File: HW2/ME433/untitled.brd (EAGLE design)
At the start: 50 x 50 mm, 19 parts, among them SW1 DIP-SLIDE-SWITCH(3P-11.6X4.0X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

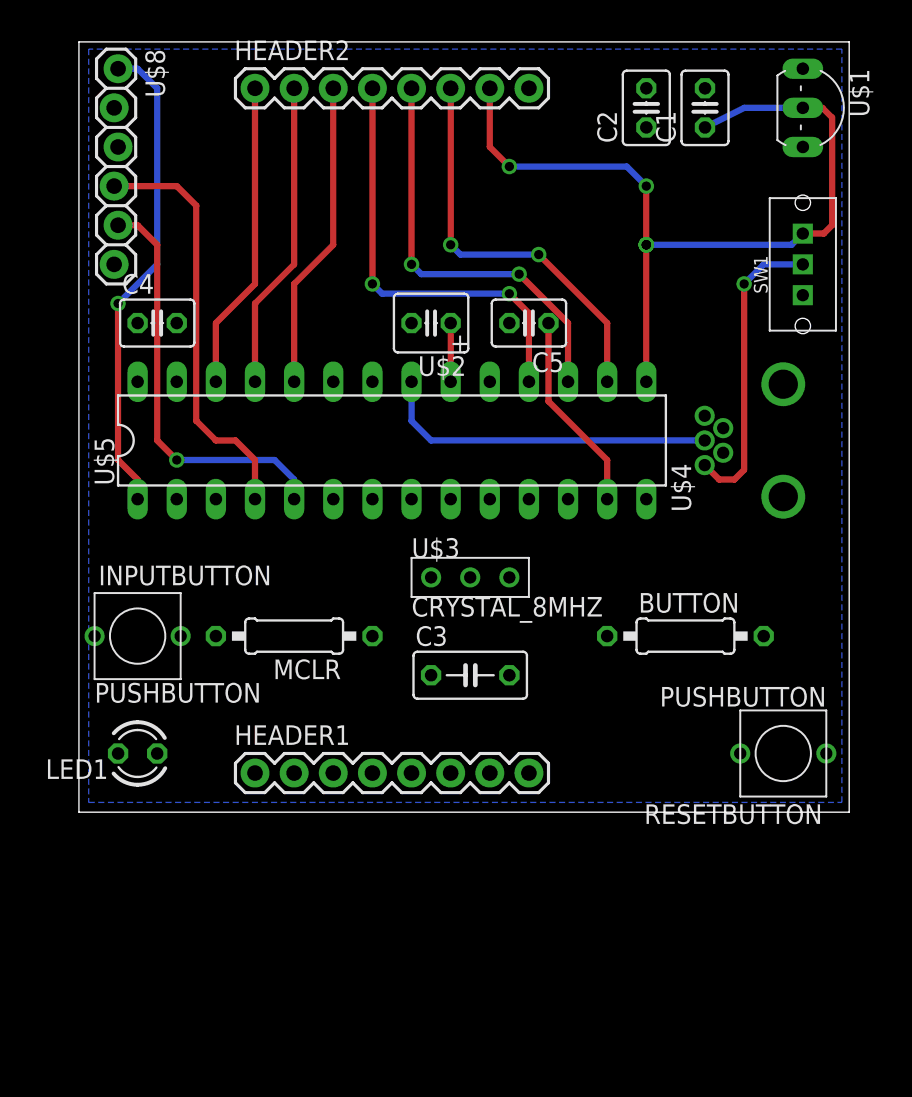
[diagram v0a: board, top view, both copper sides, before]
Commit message: wide traces
wider power traces
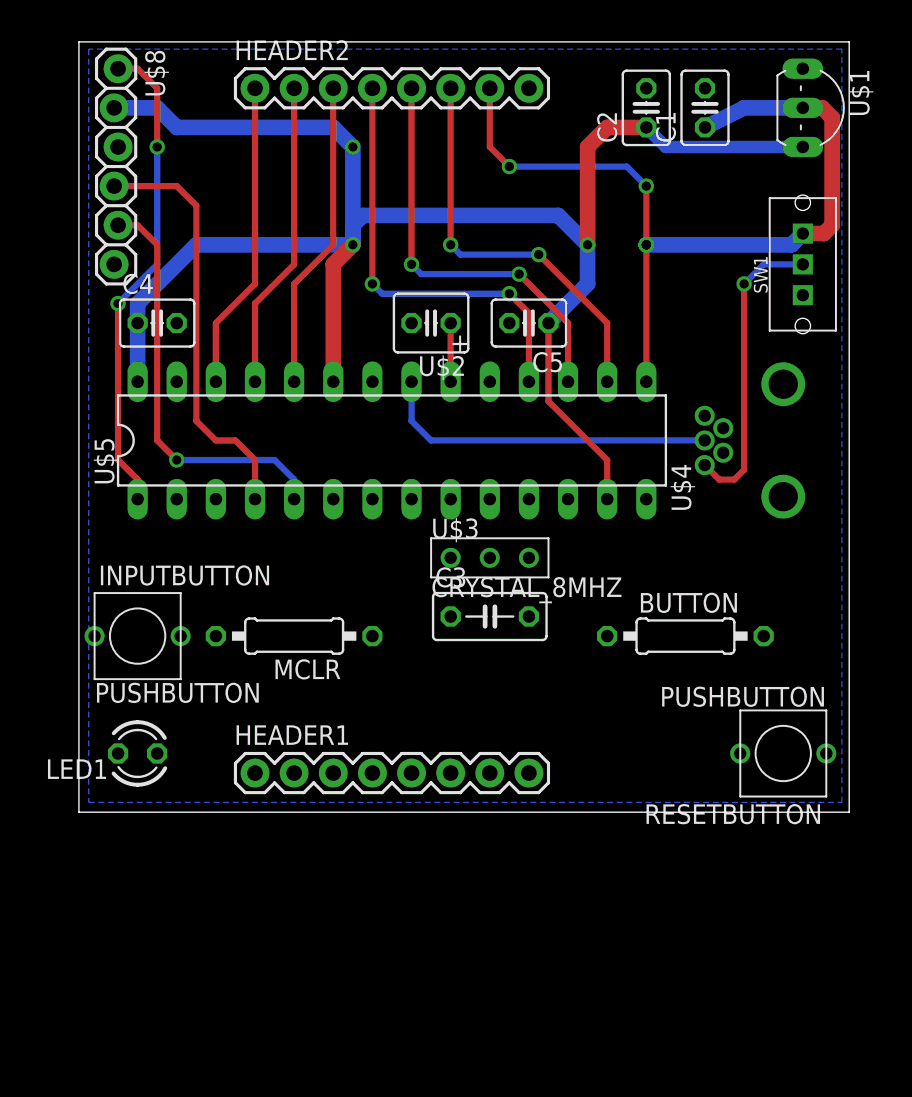
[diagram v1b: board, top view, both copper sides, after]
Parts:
- moved C3 4.02 mm to (26.7, 12.7)
- moved U$3 1.80 mm to (26.7, 16.5)
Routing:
- net +3V3: track 13.0 -> 114.8 mm, vias 0 -> 3
- net MCLR: vias 1 -> 2
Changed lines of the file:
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@@
 <element name="C1" library="components" package="C025-030X050" value="1uf" x="40.64" y="45.72" rot="R90"/>
 <element name="C2" library="components" package="C025-030X050" value="1uf" x="36.83" y="45.72" rot="R90"/>
-<element name="C3" library="components" package="C050-030X075" value=".1uf" x="25.4" y="8.89"/>
+<element name="C3" library="components" package="C050-030X075" value=".1uf" x="26.67" y="12.7"/>
 <element name="C4" library="components" package="C025-030X050" value=".1uf" x="5.08" y="31.75"/>
 <element name="C5" library="components" package="C025-030X050" value=".1uf" x="29.21" y="31.75" rot="R180"/>
@@
 <element name="U$1" library="components" package="TO92-EBC" value="VOLTAGE_REGULATOR_MCP1702" x="48.26" y="45.72" rot="R270"/>
 <element name="U$2" library="components" package="C025-040X050POL" value="CAP_TANT_10UFSHORT" x="22.86" y="31.75" rot="R180"/>
-<element name="U$3" library="components" package="CRYSTAL_8MHZ" value="CRYSTAL_8MHZ" x="25.4" y="15.24"/>
+<element name="U$3" library="components" package="CRYSTAL_8MHZ" value="CRYSTAL_8MHZ" x="26.67" y="16.51"/>
 <element name="U$4" library="components" package="USB-MB-H" value="MICROUSB_BREAKOUTUSBMICROMBH" x="45.72" y="24.13" rot="R180"/>
 <element name="U$5" library="components" package="DIL28-3" value="PIC32MX250F128B" x="20.32" y="24.13"/>
@@
 <wire x1="30.48" y1="26.67" x2="34.29" y2="22.86" width="0.4064" layer="1"/>
 <wire x1="34.29" y1="22.86" x2="34.29" y2="20.32" width="0.4064" layer="1"/>
-<wire x1="36.83" y1="44.45" x2="46.99" y2="43.18" width="0" layer="19" extent="1-1"/>
-<wire x1="30.48" y1="31.75" x2="36.83" y2="44.45" width="0" layer="19" extent="1-1"/>
-<wire x1="34.29" y1="11.43" x2="34.29" y2="20.32" width="0" layer="19" extent="1-1"/>
-<wire x1="22.86" y1="8.89" x2="34.29" y2="11.43" width="0" layer="19" extent="1-1"/>
-<wire x1="19.05" y1="11.43" x2="22.86" y2="8.89" width="0" layer="19" extent="1-1"/>
-<wire x1="26.67" y1="2.54" x2="22.86" y2="8.89" width="0" layer="19" extent="1-1"/>
-<wire x1="16.51" y1="27.94" x2="30.48" y2="26.67" width="0" layer="19" extent="1-1"/>
-<wire x1="3.81" y1="27.94" x2="16.51" y2="27.94" width="0" layer="19" extent="1-1"/>
-<wire x1="3.81" y1="31.75" x2="3.81" y2="27.94" width="0" layer="19" extent="1-1"/>
-<wire x1="2.286" y1="45.72" x2="3.81" y2="31.75" width="0" layer="19" extent="1-1"/>
+<wire x1="46.99" y1="43.18" x2="38.1" y2="43.18" width="0.8128" layer="16"/>
+<wire x1="38.1" y1="43.18" x2="36.83" y2="44.45" width="0.8128" layer="16"/>
+<wire x1="36.83" y1="44.45" x2="34.29" y2="44.45" width="1.016" layer="1"/>
+<wire x1="34.29" y1="44.45" x2="33.02" y2="43.18" width="1.016" layer="1"/>
+<wire x1="33.02" y1="43.18" x2="33.02" y2="36.83" width="1.016" layer="1"/>
+<via x="33.02" y="36.83" extent="1-16" drill="0.6"/>
+<wire x1="33.02" y1="36.83" x2="33.02" y2="34.29" width="1.016" layer="16"/>
+<wire x1="33.02" y1="34.29" x2="30.48" y2="31.75" width="1.016" layer="16"/>
+<wire x1="16.51" y1="27.94" x2="16.51" y2="35.56" width="1.016" layer="1"/>
+<wire x1="16.51" y1="35.56" x2="17.78" y2="36.83" width="1.016" layer="1"/>
+<via x="17.78" y="36.83" extent="1-16" drill="0.6"/>
+<wire x1="17.78" y1="36.83" x2="17.78" y2="38.1" width="1.016" layer="16"/>
+<wire x1="17.78" y1="38.1" x2="18.415" y2="38.735" width="1.016" layer="16"/>
+<wire x1="18.415" y1="38.735" x2="31.115" y2="38.735" width="1.016" layer="16"/>
+<wire x1="31.115" y1="38.735" x2="33.02" y2="36.83" width="1.016" layer="16"/>
+<wire x1="2.286" y1="45.72" x2="5.08" y2="45.72" width="1.016" layer="16"/>
+<wire x1="5.08" y1="45.72" x2="6.35" y2="44.45" width="1.016" layer="16"/>
+<wire x1="6.35" y1="44.45" x2="16.51" y2="44.45" width="1.016" layer="16"/>
+<wire x1="16.51" y1="44.45" x2="17.78" y2="43.18" width="1.016" layer="16"/>
+<via x="17.78" y="43.18" extent="1-16" drill="0.6"/>
+<wire x1="3.81" y1="27.94" x2="3.81" y2="31.75" width="0.4064" layer="16"/>
+<wire x1="3.81" y1="27.94" x2="3.81" y2="33.02" width="1.016" layer="16"/>
+<wire x1="3.81" y1="33.02" x2="7.62" y2="36.83" width="1.016" layer="16"/>
+<wire x1="7.62" y1="36.83" x2="17.78" y2="36.83" width="1.016" layer="16"/>
+<wire x1="34.29" y1="20.32" x2="34.29" y2="11.43" width="0" layer="19" extent="1-1"/>
+<wire x1="24.13" y1="12.7" x2="34.29" y2="11.43" width="0" layer="19" extent="1-1"/>
+<wire x1="19.05" y1="11.43" x2="24.13" y2="12.7" width="0" layer="19" extent="1-1"/>
+<wire x1="26.67" y1="2.54" x2="24.13" y2="12.7" width="0" layer="19" extent="1-1"/>
+<wire x1="17.78" y1="43.18" x2="17.78" y2="36.83" width="1.016" layer="16"/>
 </signal>
 <signal name="+5V">
@@
 <contactref element="SW1" pad="RIGHT"/>
 <contactref element="HEADER2" pad="7"/>
-<wire x1="46.99" y1="37.56" x2="46.26" y2="36.83" width="0.4064" layer="16"/>
-<wire x1="48.355" y1="37.56" x2="46.99" y2="37.56" width="0.4064" layer="1"/>
-<wire x1="40.64" y1="44.45" x2="43.18" y2="45.72" width="0.4064" layer="16"/>
-<wire x1="43.18" y1="45.72" x2="46.99" y2="45.72" width="0.4064" layer="16"/>
-<wire x1="36.83" y1="36.83" x2="46.26" y2="36.83" width="0.4064" layer="16"/>
-<wire x1="48.355" y1="37.56" x2="48.895" y2="38.1" width="0.4064" layer="1"/>
-<wire x1="48.895" y1="38.1" x2="48.895" y2="45.085" width="0.4064" layer="1"/>
-<wire x1="48.895" y1="45.085" x2="48.26" y2="45.72" width="0.4064" layer="1"/>
-<wire x1="48.26" y1="45.72" x2="46.99" y2="45.72" width="0.4064" layer="1"/>
+<wire x1="46.99" y1="37.56" x2="46.26" y2="36.83" width="1.016" layer="16"/>
+<wire x1="48.355" y1="37.56" x2="46.99" y2="37.56" width="1.016" layer="1"/>
+<wire x1="40.64" y1="44.45" x2="43.18" y2="45.72" width="1.016" layer="16"/>
+<wire x1="43.18" y1="45.72" x2="46.99" y2="45.72" width="1.016" layer="16"/>
+<wire x1="36.83" y1="36.83" x2="46.26" y2="36.83" width="1.016" layer="16"/>
+<wire x1="48.355" y1="37.56" x2="48.895" y2="38.1" width="1.016" layer="1"/>
+<wire x1="48.895" y1="38.1" x2="48.895" y2="45.085" width="1.016" layer="1"/>
+<wire x1="48.895" y1="45.085" x2="48.26" y2="45.72" width="1.016" layer="1"/>
+<wire x1="48.26" y1="45.72" x2="46.99" y2="45.72" width="1.016" layer="1"/>
 <wire x1="36.83" y1="27.94" x2="36.83" y2="36.83" width="0.4064" layer="1"/>
 <via x="36.83" y="36.83" extent="1-16" drill="0.6"/>
@@
 <contactref element="MCLR" pad="2"/>
 <contactref element="RESETBUTTON" pad="P$2"/>
-<wire x1="2.54" y1="48.26" x2="3.81" y2="48.26" width="0.4064" layer="16"/>
-<wire x1="3.81" y1="48.26" x2="5.08" y2="46.99" width="0.4064" layer="16"/>
-<wire x1="5.08" y1="46.99" x2="5.08" y2="35.56" width="0.4064" layer="16"/>
 <wire x1="5.08" y1="35.56" x2="2.54" y2="33.02" width="0.4064" layer="16"/>
 <via x="2.54" y="33.02" extent="1-16" drill="0.6"/>
@@
 <wire x1="2.54" y1="22.86" x2="3.81" y2="21.59" width="0.4064" layer="1"/>
 <wire x1="3.81" y1="21.59" x2="3.81" y2="20.32" width="0.4064" layer="1"/>
+<wire x1="2.54" y1="48.26" x2="3.81" y2="48.26" width="0.4064" layer="1"/>
+<wire x1="3.81" y1="48.26" x2="5.08" y2="46.99" width="0.4064" layer="1"/>
+<wire x1="5.08" y1="46.99" x2="5.08" y2="43.18" width="0.4064" layer="1"/>
+<via x="5.08" y="43.18" extent="1-16" drill="0.6"/>
+<wire x1="5.08" y1="43.18" x2="5.08" y2="35.56" width="0.4064" layer="16"/>
 <wire x1="8.89" y1="11.43" x2="42.926" y2="3.81" width="0" layer="19" extent="1-1"/>
 <wire x1="3.81" y1="20.32" x2="8.89" y2="11.43" width="0" layer="19" extent="1-1"/>
@@
 <contactref element="U$5" pad="9"/>
 <contactref element="U$3" pad="OSC1"/>
-<wire x1="22.86" y1="15.24" x2="24.13" y2="20.32" width="0" layer="19" extent="1-1"/>
+<wire x1="24.13" y1="16.51" x2="24.13" y2="20.32" width="0" layer="19" extent="1-1"/>
 </signal>
 <signal name="OSC2">
 <contactref element="U$5" pad="10"/>
 <contactref element="U$3" pad="OSC2"/>
-<wire x1="27.94" y1="15.24" x2="26.67" y2="20.32" width="0" layer="19" extent="1-1"/>
+<wire x1="29.21" y1="16.51" x2="26.67" y2="20.32" width="0" layer="19" extent="1-1"/>
 </signal>
 <signal name="VCAP">

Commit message: rearrange
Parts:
- moved INPUTBUTTON 41.9 mm to (45.7, 10.2), turned to 270 degrees
- moved RESETBUTTON 41.9 mm to (3.81, 5.08), turned to 90 degrees
- moved LED1 41.9 mm to (45.7, 3.81), turned to 270 degrees
- moved MCLR 5.08 mm to (8.89, 11.4)
- moved BUTTON 3.81 mm to (39.4, 15.2), turned to 180 degrees
- turned C3 to 180 degrees
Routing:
- net +3V3: track 114.8 -> 187.9 mm, vias 3 -> 7
- net B4: track 0.00 -> 48.4 mm, vias 0 -> 1
- net A4: track 0.00 -> 38.4 mm, vias 0 -> 2
- net USBD-: track 0.00 -> 31.4 mm
- net USBID: track 0.00 -> 15.1 mm
- net MCLR: track 31.3 -> 43.8 mm
- net OSC2: track 0.00 -> 4.86 mm
- net OSC1: track 0.00 -> 3.81 mm

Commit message: completed circuit no error check
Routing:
- net A1: track 0.00 -> 19.9 mm
- net A0: track 0.00 -> 19.9 mm
- net B3: track 0.00 -> 17.8 mm
- net B2: track 0.00 -> 17.8 mm
- net +3V3: track 187.9 -> 194.0 mm
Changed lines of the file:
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@@
 <wire x1="3.81" y1="27.94" x2="3.81" y2="31.75" width="0.4064" layer="16"/>
 <wire x1="3.81" y1="27.94" x2="3.81" y2="33.02" width="1.016" layer="16"/>
-<wire x1="3.81" y1="33.02" x2="7.62" y2="36.83" width="1.016" layer="16"/>
-<wire x1="7.62" y1="36.83" x2="17.78" y2="36.83" width="1.016" layer="16"/>
 <wire x1="17.78" y1="43.18" x2="17.78" y2="36.83" width="1.016" layer="16"/>
-<wire x1="46.99" y1="43.18" x2="46.99" y2="41.91" width="0.4064" layer="16"/>
-<wire x1="46.99" y1="41.91" x2="45.72" y2="40.64" width="0.4064" layer="16"/>
-<wire x1="45.72" y1="40.64" x2="40.64" y2="40.64" width="0.4064" layer="16"/>
-<wire x1="40.64" y1="40.64" x2="38.735" y2="38.735" width="0.4064" layer="16"/>
+<wire x1="41.91" y1="41.91" x2="38.735" y2="38.735" width="1.016" layer="16"/>
 <via x="38.735" y="38.735" extent="1-16" drill="0.6"/>
-<wire x1="38.735" y1="38.735" x2="38.735" y2="16.51" width="0.4064" layer="1"/>
-<wire x1="38.735" y1="16.51" x2="38.735" y2="11.43" width="0.4064" layer="1"/>
-<wire x1="38.735" y1="11.43" x2="36.83" y2="9.525" width="0.4064" layer="1"/>
+<wire x1="38.735" y1="38.735" x2="38.735" y2="16.51" width="1.016" layer="1"/>
+<wire x1="38.735" y1="16.51" x2="38.735" y2="11.43" width="1.016" layer="1"/>
+<wire x1="38.735" y1="11.43" x2="36.83" y2="9.525" width="1.016" layer="1"/>
 <via x="36.83" y="9.525" extent="1-16" drill="0.6"/>
-<wire x1="36.83" y1="9.525" x2="30.48" y2="9.525" width="0.4064" layer="16"/>
-<wire x1="30.48" y1="9.525" x2="27.94" y2="9.525" width="0.4064" layer="16"/>
-<wire x1="27.94" y1="9.525" x2="15.875" y2="9.525" width="0.4064" layer="16"/>
-<wire x1="15.875" y1="9.525" x2="13.97" y2="11.43" width="0.4064" layer="16"/>
-<wire x1="29.21" y1="12.7" x2="29.21" y2="10.795" width="0.4064" layer="16"/>
-<wire x1="29.21" y1="10.795" x2="30.48" y2="9.525" width="0.4064" layer="16"/>
-<wire x1="26.67" y1="2.54" x2="26.67" y2="8.255" width="0.4064" layer="1"/>
-<wire x1="26.67" y1="8.255" x2="27.94" y2="9.525" width="0.4064" layer="1"/>
+<wire x1="36.83" y1="9.525" x2="30.48" y2="9.525" width="1.016" layer="16"/>
+<wire x1="30.48" y1="9.525" x2="27.94" y2="9.525" width="1.016" layer="16"/>
+<wire x1="27.94" y1="9.525" x2="15.875" y2="9.525" width="1.016" layer="16"/>
+<wire x1="15.875" y1="9.525" x2="13.97" y2="11.43" width="1.016" layer="16"/>
+<wire x1="29.21" y1="12.7" x2="29.21" y2="10.795" width="1.016" layer="16"/>
+<wire x1="29.21" y1="10.795" x2="30.48" y2="9.525" width="1.016" layer="16"/>
+<wire x1="26.67" y1="2.54" x2="26.67" y2="8.255" width="1.016" layer="1"/>
+<wire x1="26.67" y1="8.255" x2="27.94" y2="9.525" width="1.016" layer="1"/>
 <via x="27.94" y="9.525" extent="1-16" drill="0.6"/>
 <wire x1="44.45" y1="15.24" x2="44.45" y2="16.51" width="0.4064" layer="16"/>
@@
 <wire x1="40.005" y1="17.78" x2="38.735" y2="16.51" width="0.4064" layer="16"/>
 <via x="38.735" y="16.51" extent="1-16" drill="0.6"/>
-<wire x1="40.64" y1="40.64" x2="36.83" y2="44.45" width="0" layer="19" extent="16-16"/>
+<wire x1="36.83" y1="44.45" x2="36.83" y2="43.18" width="1.016" layer="16"/>
+<wire x1="36.83" y1="43.18" x2="38.1" y2="41.91" width="1.016" layer="16"/>
+<wire x1="38.1" y1="41.91" x2="41.91" y2="41.91" width="1.016" layer="16"/>
+<wire x1="46.99" y1="43.18" x2="43.18" y2="43.18" width="1.016" layer="16"/>
+<wire x1="43.18" y1="43.18" x2="41.91" y2="41.91" width="1.016" layer="16"/>
+<wire x1="17.78" y1="36.83" x2="15.24" y2="34.29" width="1.016" layer="16"/>
+<wire x1="15.24" y1="34.29" x2="5.08" y2="34.29" width="1.016" layer="16"/>
+<wire x1="5.08" y1="34.29" x2="3.81" y2="33.02" width="1.016" layer="16"/>
 </signal>
 <signal name="+5V">
@@
 <contactref element="U$5" pad="2"/>
 <contactref element="HEADER1" pad="1"/>
-<wire x1="11.43" y1="2.54" x2="6.35" y2="20.32" width="0" layer="19" extent="1-1"/>
+<wire x1="11.43" y1="2.54" x2="11.43" y2="8.89" width="0.4064" layer="1"/>
+<wire x1="11.43" y1="8.89" x2="6.35" y2="13.97" width="0.4064" layer="1"/>
+<wire x1="6.35" y1="13.97" x2="6.35" y2="20.32" width="0.4064" layer="1"/>
 </signal>
 <signal name="A1">
 <contactref element="U$5" pad="3"/>
 <contactref element="HEADER1" pad="2"/>
-<wire x1="13.97" y1="2.54" x2="8.89" y2="20.32" width="0" layer="19" extent="1-1"/>
+<wire x1="8.89" y1="20.32" x2="8.89" y2="13.97" width="0.4064" layer="1"/>
+<wire x1="8.89" y1="13.97" x2="13.97" y2="8.89" width="0.4064" layer="1"/>
+<wire x1="13.97" y1="8.89" x2="13.97" y2="2.54" width="0.4064" layer="1"/>
 </signal>
 <signal name="B2">
 <contactref element="U$5" pad="6"/>
 <contactref element="HEADER1" pad="3"/>
-<wire x1="16.51" y1="2.54" x2="16.51" y2="20.32" width="0" layer="19" extent="1-1"/>
+<wire x1="16.51" y1="2.54" x2="16.51" y2="20.32" width="0.4064" layer="1"/>
 </signal>
 <signal name="B3">
 <contactref element="U$5" pad="7"/>
 <contactref element="HEADER1" pad="4"/>
-<wire x1="19.05" y1="2.54" x2="19.05" y2="20.32" width="0" layer="19" extent="1-1"/>
+<wire x1="19.05" y1="20.32" x2="19.05" y2="2.54" width="0.4064" layer="1"/>
 </signal>
 <signal name="B15">
